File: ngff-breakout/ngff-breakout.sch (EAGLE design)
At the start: 78 parts, among them U2 LD1085D2T33R, X1 PINHD-2X4, X3 694108106102, X8 ZX360D-B-10P(30), Y1 MHF4, Y2 MHF4, Y3 MHF4

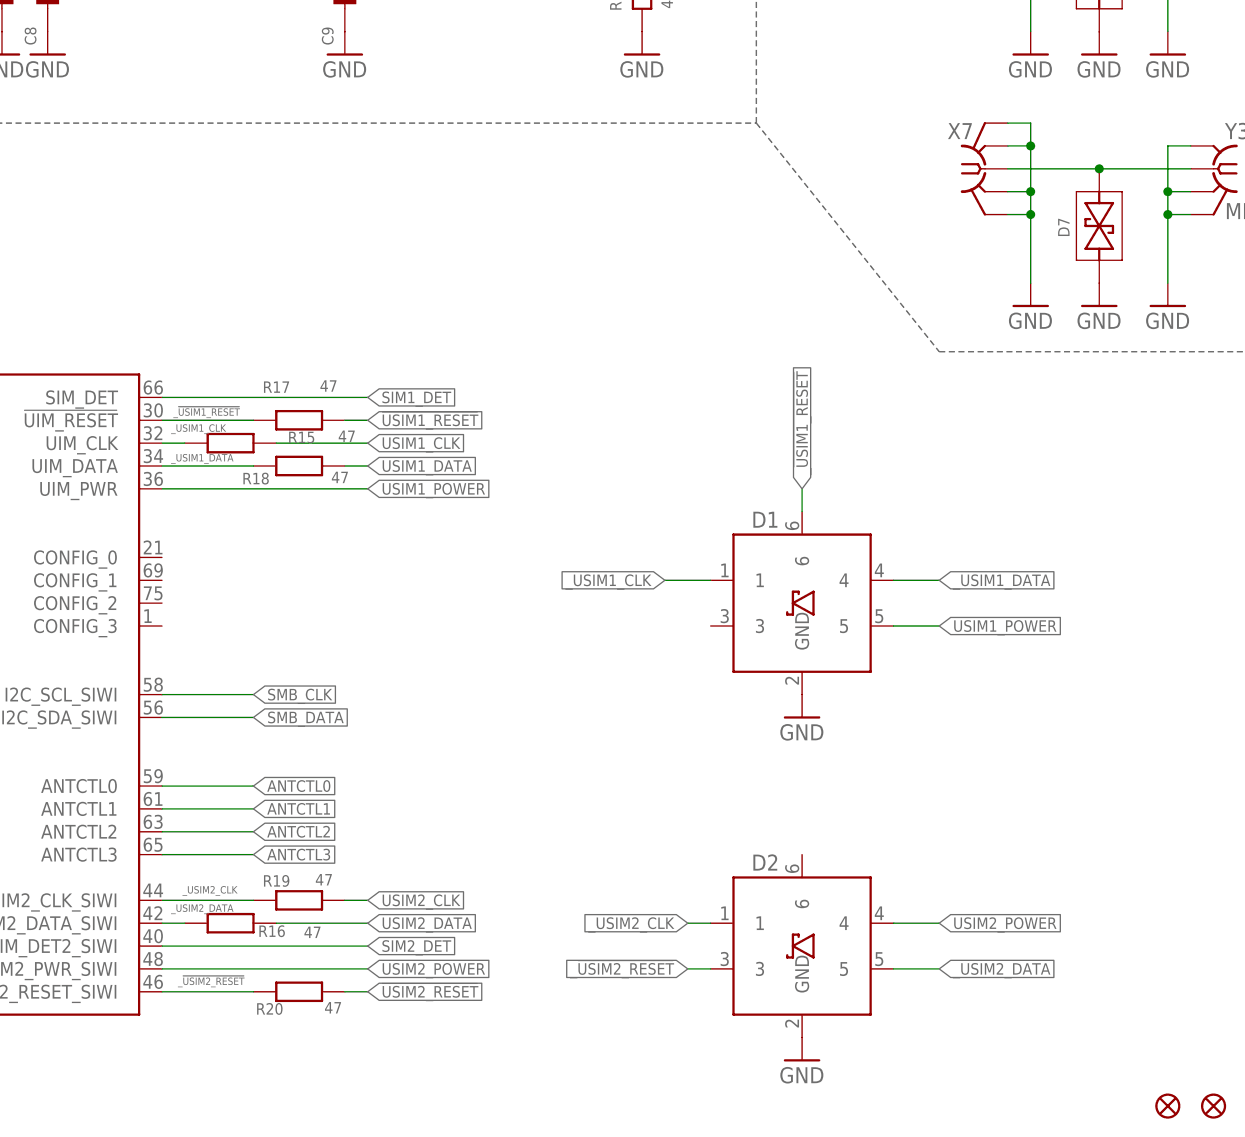
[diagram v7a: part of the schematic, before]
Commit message: ngff: make room for 2x5 header and route SIM2 signals there
adresses OS#4211
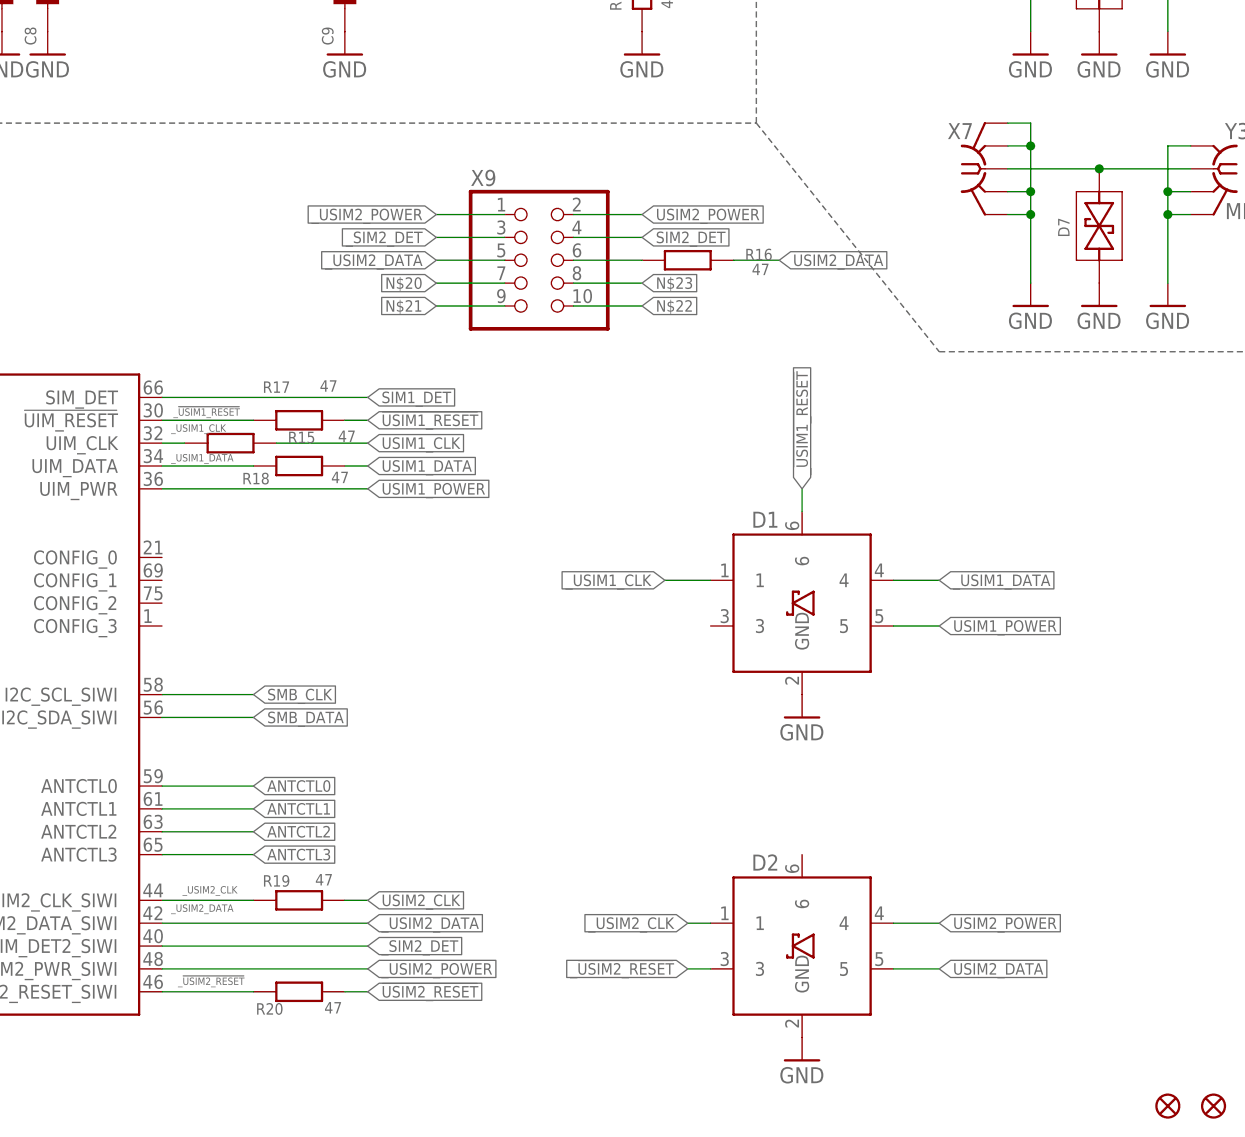
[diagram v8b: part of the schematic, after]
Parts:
- added X9: (no value), laforge:PINHD-2X5
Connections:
- new net N$15: R16.1, X9.6
- new net N$20: X9.7
- new net N$21: X9.9
- new net N$22: X9.10
- new net N$23: X9.8
- new net _SIM2_DET: NGFF1G$1.I2C_SCL_HW/SIM_DET2_SIWI, X9.3
- new net _USIM2_POWER: NGFF1G$1.TX_BLANKING_HW/UIM2_PWR_SIWI, X9.1
- net SIM2_DET: now also X9.4; no longer NGFF1G$1.I2C_SCL_HW/SIM_DET2_SIWI
- net USIM2_DATA: now also D2.5
- net USIM2_POWER: now also X9.2; no longer NGFF1G$1.TX_BLANKING_HW/UIM2_PWR_SIWI
- net _USIM2_DATA: now also X9.5; no longer D2.5, R16.1
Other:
- moved on the sheet: R16
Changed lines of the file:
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@@
 <part name="GND21" library="supply1" deviceset="GND" device=""/>
 <part name="GND28" library="supply1" deviceset="GND" device=""/>
+<part name="X9" library="laforge" deviceset="PINHD-2X5" device=""/>
 </parts>
 <sheets>
@@
 <attribute name="VALUE" x="182.118" y="32.131" size="1.27" layer="96"/>
 </instance>
-<instance part="R16" gate="G$1" x="172.72" y="27.94" smashed="yes">
-<attribute name="DESCRIPTION" x="172.72" y="27.94" size="1.778" layer="96" display="off"/>
-<attribute name="MANUFACTURER" x="172.72" y="27.94" size="1.778" layer="96" display="off"/>
-<attribute name="MANUFACTURERPARTNUMBER" x="172.72" y="27.94" size="1.778" layer="96" display="off"/>
-<attribute name="SOURCE" x="172.72" y="27.94" size="1.778" layer="96" display="off"/>
-<attribute name="SOURCEPARTNUMBER" x="172.72" y="27.94" size="1.778" layer="96" display="off"/>
-<attribute name="ROHSCERTIFICATE" x="172.72" y="27.94" size="1.778" layer="96" display="off"/>
-<attribute name="POPULATED" x="172.72" y="27.94" size="1.778" layer="96" display="off"/>
-<attribute name="CLASS" x="172.72" y="27.94" size="1.778" layer="96" display="off"/>
-<attribute name="LINK" x="172.72" y="27.94" size="1.778" layer="96" display="off"/>
-<attribute name="NAME" x="175.768" y="26.416" size="1.27" layer="95"/>
-<attribute name="VALUE" x="180.848" y="26.289" size="1.27" layer="96"/>
+<instance part="R16" gate="G$1" x="223.52" y="101.6" smashed="yes">
+<attribute name="DESCRIPTION" x="223.52" y="101.6" size="1.778" layer="96" display="off"/>
+<attribute name="MANUFACTURER" x="223.52" y="101.6" size="1.778" layer="96" display="off"/>
+<attribute name="MANUFACTURERPARTNUMBER" x="223.52" y="101.6" size="1.778" layer="96" display="off"/>
+<attribute name="SOURCE" x="223.52" y="101.6" size="1.778" layer="96" display="off"/>
+<attribute name="SOURCEPARTNUMBER" x="223.52" y="101.6" size="1.778" layer="96" display="off"/>
+<attribute name="ROHSCERTIFICATE" x="223.52" y="101.6" size="1.778" layer="96" display="off"/>
+<attribute name="POPULATED" x="223.52" y="101.6" size="1.778" layer="96" display="off"/>
+<attribute name="CLASS" x="223.52" y="101.6" size="1.778" layer="96" display="off"/>
+<attribute name="LINK" x="223.52" y="101.6" size="1.778" layer="96" display="off"/>
+<attribute name="NAME" x="229.87" y="101.6" size="1.27" layer="95"/>
+<attribute name="VALUE" x="230.632" y="99.949" size="1.27" layer="96"/>
 </instance>
 <instance part="SIM2" gate="-CARD" x="167.64" y="134.62" smashed="yes">
@@
 <instance part="GND21" gate="1" x="109.22" y="124.46"/>
 <instance part="GND28" gate="1" x="218.44" y="124.46"/>
+<instance part="X9" gate="A" x="205.74" y="101.6"/>
 </instances>
 <busses>
@@
 <segment>
 <pinref part="NGFF1" gate="G$1" pin="I2C_SDA_HW/UIM2_DATA_SIWI"/>
-<pinref part="R16" gate="G$1" pin="1"/>
-<wire x1="167.64" y1="27.94" x2="165.1" y2="27.94" width="0.1524" layer="91"/>
+<wire x1="187.96" y1="27.94" x2="165.1" y2="27.94" width="0.1524" layer="91"/>
 <label x="166.116" y="29.21" size="0.8128" layer="95"/>
-</segment>
-<segment>
-<pinref part="D2" gate="G$1" pin="5"/>
-<wire x1="246.38" y1="22.86" x2="251.46" y2="22.86" width="0.1524" layer="91"/>
-<label x="251.46" y="22.86" size="1.27" layer="95" xref="yes"/>
+<label x="187.96" y="27.94" size="1.27" layer="95" xref="yes"/>
+</segment>
+<segment>
+<pinref part="X9" gate="A" pin="5"/>
+<wire x1="203.2" y1="101.6" x2="195.58" y2="101.6" width="0.1524" layer="91"/>
+<label x="195.58" y="101.6" size="1.27" layer="95" rot="R180" xref="yes"/>
 </segment>
 </net>
 <net name="SIM2_DET" class="0">
-<segment>
-<pinref part="NGFF1" gate="G$1" pin="I2C_SCL_HW/SIM_DET2_SIWI"/>
-<wire x1="165.1" y1="25.4" x2="187.96" y2="25.4" width="0.1524" layer="91"/>
-<label x="187.96" y="25.4" size="1.27" layer="95" xref="yes"/>
-</segment>
 <segment>
 <pinref part="SIM2" gate="-DETECT" pin="0@A"/>
@@
 <junction x="218.44" y="137.16"/>
 </segment>
+<segment>
+<pinref part="X9" gate="A" pin="4"/>
+<wire x1="210.82" y1="104.14" x2="218.44" y2="104.14" width="0.1524" layer="91"/>
+<label x="218.44" y="104.14" size="1.27" layer="95" xref="yes"/>
+</segment>
 </net>
 <net name="USIM2_POWER" class="0">
-<segment>
-<pinref part="NGFF1" gate="G$1" pin="TX_BLANKING_HW/UIM2_PWR_SIWI"/>
-<wire x1="165.1" y1="22.86" x2="187.96" y2="22.86" width="0.1524" layer="91"/>
-<label x="187.96" y="22.86" size="1.27" layer="95" xref="yes"/>
-</segment>
 <segment>
 <pinref part="SIM2" gate="-CARD" pin="VCC"/>
@@
 <label x="251.46" y="27.94" size="1.27" layer="95" xref="yes"/>
 </segment>
+<segment>
+<pinref part="X9" gate="A" pin="2"/>
+<wire x1="210.82" y1="106.68" x2="218.44" y2="106.68" width="0.1524" layer="91"/>
+<label x="218.44" y="106.68" size="1.27" layer="95" xref="yes"/>
+</segment>
 </net>
 <net name="_!USIM2_RESET" class="0">
@@
 <segment>
 <pinref part="R16" gate="G$1" pin="2"/>
-<wire x1="177.8" y1="27.94" x2="187.96" y2="27.94" width="0.1524" layer="91"/>
-<label x="187.96" y="27.94" size="1.27" layer="95" xref="yes"/>
+<wire x1="228.6" y1="101.6" x2="233.68" y2="101.6" width="0.1524" layer="91"/>
+<label x="233.68" y="101.6" size="1.27" layer="95" xref="yes"/>
 </segment>
 <segment>
@@
 <wire x1="154.94" y1="147.32" x2="157.48" y2="147.32" width="0.1524" layer="91"/>
 <label x="157.48" y="147.32" size="1.27" layer="95" xref="yes"/>
+</segment>
+<segment>
+<pinref part="D2" gate="G$1" pin="5"/>
+<wire x1="246.38" y1="22.86" x2="251.46" y2="22.86" width="0.1524" layer="91"/>
+<label x="251.46" y="22.86" size="1.27" layer="95" xref="yes"/>
 </segment>
 </net>
@@
 </segment>
 </net>
+<net name="N$20" class="0">
+<segment>
+<pinref part="X9" gate="A" pin="7"/>
+<wire x1="203.2" y1="99.06" x2="195.58" y2="99.06" width="0.1524" layer="91"/>
+<label x="195.58" y="99.06" size="1.27" layer="95" rot="R180" xref="yes"/>
+</segment>
+</net>
+<net name="N$21" class="0">
+<segment>
+<pinref part="X9" gate="A" pin="9"/>
+<wire x1="203.2" y1="96.52" x2="195.58" y2="96.52" width="0.1524" layer="91"/>
+<label x="195.58" y="96.52" size="1.27" layer="95" rot="R180" xref="yes"/>
+</segment>
+</net>
+<net name="N$22" class="0">
+<segment>
+<pinref part="X9" gate="A" pin="10"/>
+<wire x1="210.82" y1="96.52" x2="218.44" y2="96.52" width="0.1524" layer="91"/>
+<label x="218.44" y="96.52" size="1.27" layer="95" xref="yes"/>
+</segment>
+</net>
+<net name="N$23" class="0">
+<segment>
+<pinref part="X9" gate="A" pin="8"/>
+<wire x1="210.82" y1="99.06" x2="218.44" y2="99.06" width="0.1524" layer="91"/>
+<label x="218.44" y="99.06" size="1.27" layer="95" xref="yes"/>
+</segment>
+</net>
+<net name="_USIM2_POWER" class="0">
+<segment>
+<pinref part="NGFF1" gate="G$1" pin="TX_BLANKING_HW/UIM2_PWR_SIWI"/>
+<wire x1="165.1" y1="22.86" x2="187.96" y2="22.86" width="0.1524" layer="91"/>
+<label x="187.96" y="22.86" size="1.27" layer="95" xref="yes"/>
+</segment>
+<segment>
+<pinref part="X9" gate="A" pin="1"/>
+<wire x1="203.2" y1="106.68" x2="195.58" y2="106.68" width="0.1524" layer="91"/>
+<label x="195.58" y="106.68" size="1.27" layer="95" rot="R180" xref="yes"/>
+</segment>
+</net>
+<net name="_SIM2_DET" class="0">
+<segment>
+<pinref part="NGFF1" gate="G$1" pin="I2C_SCL_HW/SIM_DET2_SIWI"/>
+<wire x1="165.1" y1="25.4" x2="187.96" y2="25.4" width="0.1524" layer="91"/>
+<label x="187.96" y="25.4" size="1.27" layer="95" xref="yes"/>
+</segment>
+<segment>
+<pinref part="X9" gate="A" pin="3"/>
+<wire x1="203.2" y1="104.14" x2="195.58" y2="104.14" width="0.1524" layer="91"/>
+<label x="195.58" y="104.14" size="1.27" layer="95" rot="R180" xref="yes"/>
+</segment>
+</net>
+<net name="N$15" class="0">
+<segment>
+<pinref part="R16" gate="G$1" pin="1"/>
+<pinref part="X9" gate="A" pin="6"/>
+<wire x1="218.44" y1="101.6" x2="210.82" y2="101.6" width="0.1524" layer="91"/>
+</segment>
+</net>
